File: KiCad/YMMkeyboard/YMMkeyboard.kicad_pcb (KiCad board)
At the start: 2 copper layers, 100 x 100 mm, 65 parts, among them J2 Conn_01x09, J3 Conn_01x09, SW10 SW_Push, SW11 SW_Push, SW12 SW_Push, SW13 SW_Push, SW14 SW_Push, SW15 SW_Push, SW16 SW_Push, SW17 SW_Push, SW18 SW_Push, SW19 SW_Push, SW2 SW_Push, SW20 SW_Push, SW21 SW_Push, SW22 SW_Push, SW23 SW_Push, SW24 SW_Push, SW25 SW_Push, SW26 SW_Push, SW27 SW_Push, SW28 SW_Push, SW29 SW_Push, SW3 SW_Push, SW30 SW_Push, SW31 SW_Push, SW32 RotaryEncoder_Switch, SW4 SW_Push, SW5 SW_Push, SW6 SW_Push, SW7 SW_Push, SW8 SW_Push, SW9 SW_Push

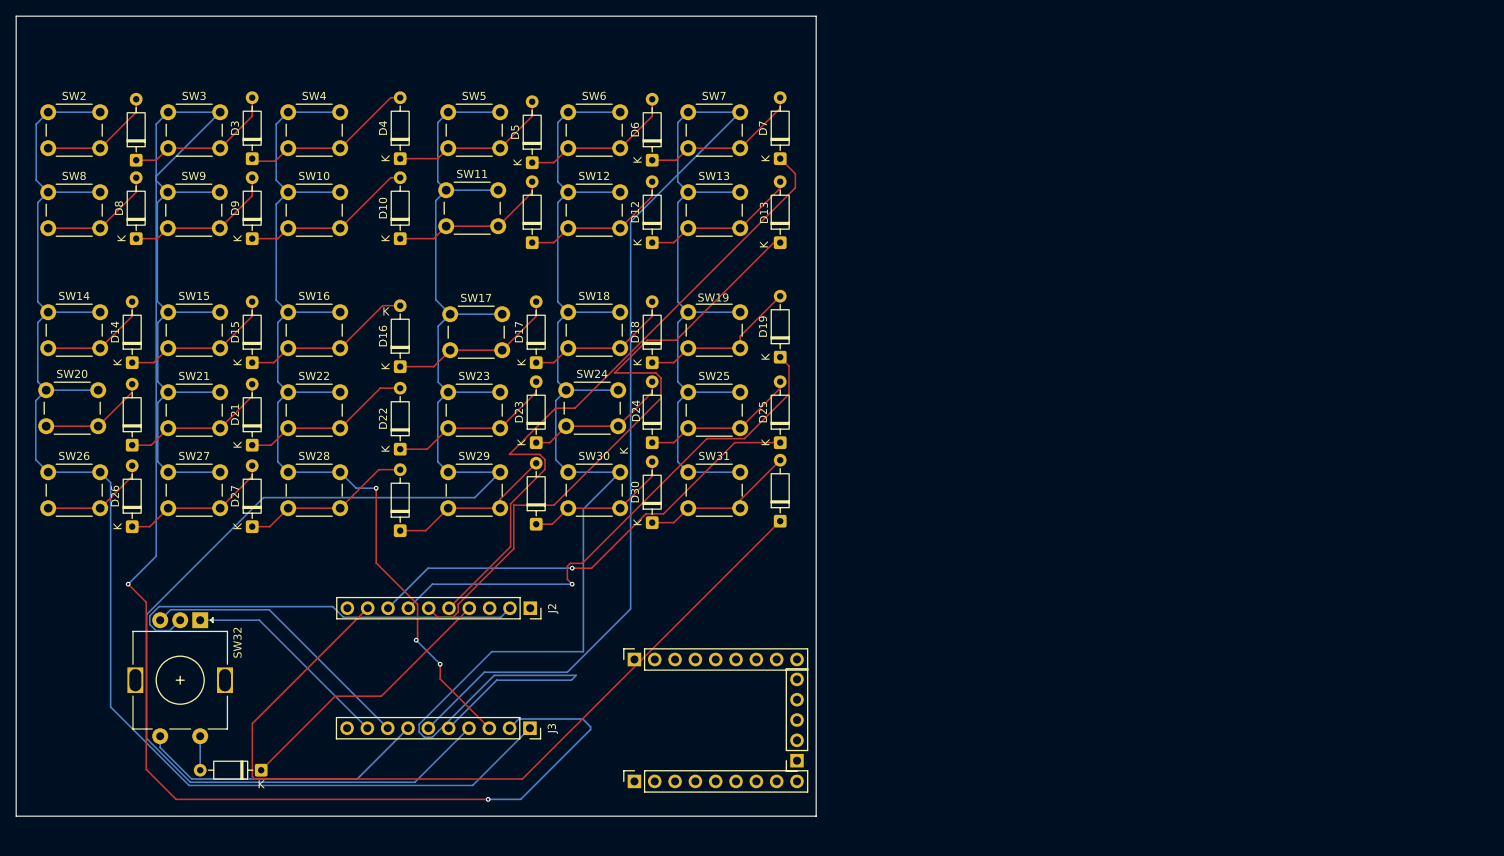
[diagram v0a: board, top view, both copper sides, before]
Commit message: キーボードの設計ミスを変更 原因:ダイオードを直列に配置した結果電圧降下した
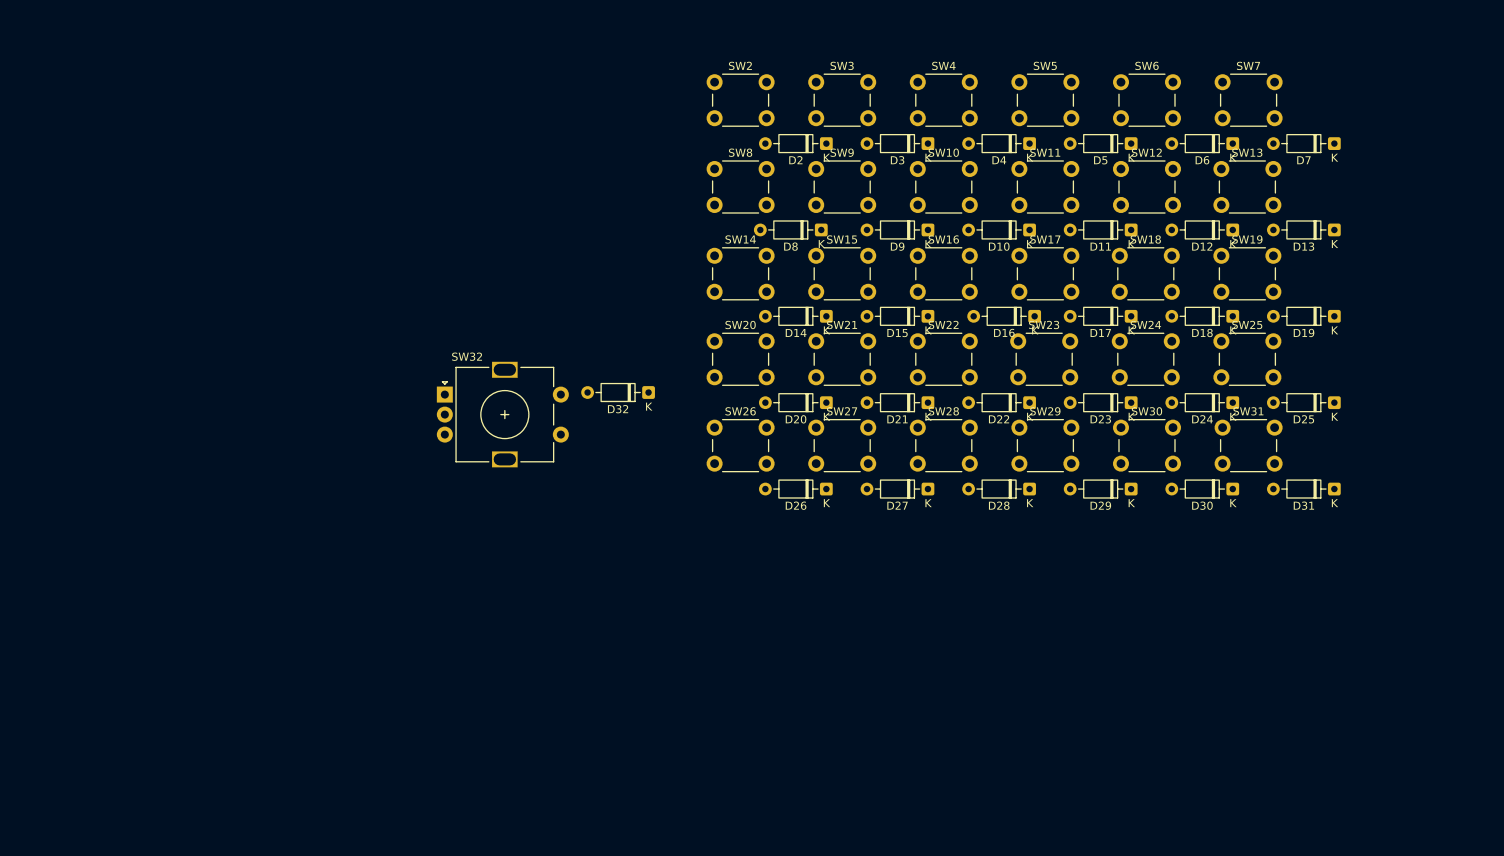
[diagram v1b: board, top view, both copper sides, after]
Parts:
- removed J2, J3: Conn_01x09, Connector_PinSocket_2.54mm:PinSocket_1x10_P2.54mm_Vertical
- removed REF**: RP2040-ZeroSocket, RP2040-ZeroSocket:RP2040-ZeroSocket
- moved D14 87.0 mm to (128.3, 56.5), turned to 180 degrees
- moved D20 86.9 mm to (128.3, 67.3), turned to 180 degrees
- moved D26 86.9 mm to (128.3, 78.1), turned to 180 degrees
- moved D2 86.3 mm to (128.3, 34.9), turned to 180 degrees
- moved D8 85.6 mm to (127.6, 45.7), turned to 180 degrees
- moved D15 84.7 mm to (141.0, 56.5), turned to 180 degrees
- moved D21 84.6 mm to (141.0, 67.3), turned to 180 degrees
- moved D27 84.6 mm to (141.0, 78.1), turned to 180 degrees
- moved D3 84.5 mm to (141.0, 34.9), turned to 180 degrees
- moved D9 84.5 mm to (141.0, 45.7), turned to 180 degrees
- moved SW20 83.8 mm to (114.3, 59.6)
- moved SW14 83.6 mm to (114.3, 49.0)
- moved SW26 83.5 mm to (114.3, 70.4)
- moved SW2 83.4 mm to (114.3, 27.2)
- moved SW8 83.4 mm to (114.3, 38.1)
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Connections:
- SW32 pad C: Net-(J2-Pin_2) -> GND
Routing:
- net Net-(SW15-Pad1): track 241.9 -> 0.00 mm, vias 2 -> 0
- net Net-(SW11-Pad1): track 194.4 -> 0.00 mm
- net Net-(SW13-Pad1): track 181.0 -> 0.00 mm
- net Net-(SW12-Pad1): track 173.2 -> 0.00 mm
- net Net-(SW14-Pad1): track 171.3 -> 0.00 mm
- net Net-(SW10-Pad1): track 123.5 -> 0.00 mm, vias 3 -> 0
- net Net-(D31-K): track 106.5 -> 0.00 mm
- net Net-(D7-K): track 82.3 -> 0.00 mm
- net Net-(D13-K): track 80.6 -> 0.00 mm
- net Net-(D19-K): track 65.9 -> 0.00 mm, vias 1 -> 0
- net Net-(D25-K): track 57.6 -> 0.00 mm, vias 1 -> 0
- net Net-(J2-Pin_2): track 52.3 -> 0.00 mm
- net Net-(SW32-PadS1): track 36.7 -> 0.00 mm
- net Net-(SW32-PadB): track 35.1 -> 0.00 mm
- net Net-(D32-K): track 34.4 -> 0.00 mm
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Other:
- board outline removed

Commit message: 2号機発注データ
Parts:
- removed the D29 at (166.4, 78.1)
- added D29: 1N4148, Diode_THT:D_DO-35_SOD27_P7.62mm_Horizontal, F.Cu at (175.2, 92.0)
- added D29: 1N4148, Diode_THT:D_DO-35_SOD27_P7.62mm_Horizontal, F.Cu at (174.3, 65.1)
- added J1: OLED, Connector_PinSocket_2.54mm:PinSocket_1x05_P2.54mm_Vertical, F.Cu at (167.0, 81.9)
- added J3: RGB, Connector_PinSocket_2.54mm:PinSocket_1x03_P2.54mm_Vertical, F.Cu at (204.0, 83.5)
- added REF**: KEY_SWITCH, isw-kbd:CherryMX_Hotswap_1u, F.Cu at (181.0, 87.0)
- added U1: RP2040-Zero, RP2040-ZeroSocket:RP2040-ZeroSocket, F.Cu at (125.7, 108.3)
- moved SW32 113.8 mm to (186.5, 108.0)
- moved D32 113.5 mm to (208.0, 116.0), turned to 90 degrees
- moved D31 17.4 mm to (203.3, 65.1), turned to -90 degrees
- moved D25 16.8 mm to (203.3, 55.1), turned to -90 degrees
- moved D30 16.6 mm to (189.3, 65.1), turned to -90 degrees
- moved D19 16.2 mm to (203.3, 45.1), turned to -90 degrees
- moved SW25 16.0 mm to (193.5, 57.2)
- moved SW31 16.0 mm to (193.5, 67.3)
- moved D24 15.9 mm to (189.3, 55.1), turned to -90 degrees
- moved SW19 15.9 mm to (193.5, 47.0)
- moved SW13 15.9 mm to (193.5, 36.8)
- moved SW7 15.7 mm to (193.5, 26.7)
- moved D13 15.5 mm to (203.0, 35.0), turned to -90 degrees
- moved D18 15.3 mm to (189.3, 45.1), turned to -90 degrees
- moved D7 15.2 mm to (203.3, 25.1), turned to -90 degrees
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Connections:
- D11 pad 1: Net-(D11-K) -> Net-(D10-K)
- D11 pad 2: Net-(D10-K) -> Net-(D11-A)
- D12 pad 1: Net-(D12-K) -> Net-(D10-K)
- D12 pad 2: Net-(D11-K) -> Net-(D12-A)
- D13 pad 1: Net-(D13-K) -> Net-(D10-K)
- D13 pad 2: Net-(D12-K) -> Net-(D13-A)
- D15 pad 1: Net-(D15-K) -> Net-(D14-K)
- D15 pad 2: Net-(D14-K) -> Net-(D15-A)
- D16 pad 1: Net-(D16-K) -> Net-(D14-K)
- D16 pad 2: Net-(D15-K) -> Net-(D16-A)
- D17 pad 1: Net-(D17-K) -> Net-(D14-K)
- D17 pad 2: Net-(D16-K) -> Net-(D17-A)
- D18 pad 1: Net-(D18-K) -> Net-(D14-K)
- D18 pad 2: Net-(D17-K) -> Net-(D18-A)
- D19 pad 1: Net-(D19-K) -> Net-(D14-K)
- D19 pad 2: Net-(D18-K) -> Net-(D19-A)
- D21 pad 1: Net-(D21-K) -> Net-(D20-K)
- D21 pad 2: Net-(D20-K) -> Net-(D21-A)
- D22 pad 1: Net-(D22-K) -> Net-(D20-K)
- D22 pad 2: Net-(D21-K) -> Net-(D22-A)
- D23 pad 1: Net-(D23-K) -> Net-(D20-K)
- D23 pad 2: Net-(D22-K) -> Net-(D23-A)
- D24 pad 1: Net-(D24-K) -> Net-(D20-K)
- D24 pad 2: Net-(D23-K) -> Net-(D24-A)
- D25 pad 1: Net-(D25-K) -> Net-(D20-K)
- D25 pad 2: Net-(D24-K) -> Net-(D25-A)
- D27 pad 1: Net-(D27-K) -> Net-(D26-K)
- D27 pad 2: Net-(D26-K) -> Net-(D27-A)
- D28 pad 1: Net-(D28-K) -> Net-(D26-K)
- D28 pad 2: Net-(D27-K) -> Net-(D28-A)
- D3 pad 1: Net-(D3-K) -> Net-(D2-K)
- D3 pad 2: Net-(D2-K) -> Net-(D3-A)
- D30 pad 1: Net-(D30-K) -> Net-(D26-K)
- D31 pad 1: Net-(D31-K) -> Net-(D26-K)
- D31 pad 2: Net-(D30-K) -> Net-(D31-A)
- D4 pad 1: Net-(D4-K) -> Net-(D2-K)
- D4 pad 2: Net-(D3-K) -> Net-(D4-A)
- D5 pad 1: Net-(D5-K) -> Net-(D2-K)
- D5 pad 2: Net-(D4-K) -> Net-(D5-A)
- D6 pad 1: Net-(D6-K) -> Net-(D2-K)
- D6 pad 2: Net-(D5-K) -> Net-(D6-A)
- D7 pad 1: Net-(D7-K) -> Net-(D2-K)
- D7 pad 2: Net-(D6-K) -> Net-(D7-A)
- D8 pad 1: Net-(D8-K) -> Net-(D10-K)
- D9 pad 1: Net-(D10-A) -> Net-(D10-K)
- D9 pad 2: Net-(D8-K) -> Net-(D9-A)
- SW11 pad 2: Net-(D10-K) -> Net-(D11-A)
- SW12 pad 2: Net-(D11-K) -> Net-(D12-A)
- SW13 pad 2: Net-(D12-K) -> Net-(D13-A)
- SW15 pad 2: Net-(D14-K) -> Net-(D15-A)
- SW16 pad 2: Net-(D15-K) -> Net-(D16-A)
- SW17 pad 2: Net-(D16-K) -> Net-(D17-A)
- SW18 pad 2: Net-(D17-K) -> Net-(D18-A)
- SW19 pad 2: Net-(D18-K) -> Net-(D19-A)
- SW21 pad 2: Net-(D20-K) -> Net-(D21-A)
- SW22 pad 2: Net-(D21-K) -> Net-(D22-A)
- SW23 pad 2: Net-(D22-K) -> Net-(D23-A)
- SW24 pad 2: Net-(D23-K) -> Net-(D24-A)
- SW25 pad 2: Net-(D24-K) -> Net-(D25-A)
- SW27 pad 2: Net-(D26-K) -> Net-(D27-A)
- SW28 pad 2: Net-(D27-K) -> Net-(D28-A)
- SW29 pad 2: Net-(D28-K) -> Net-(D29-A)
- SW3 pad 2: Net-(D2-K) -> Net-(D3-A)
- SW31 pad 2: Net-(D30-K) -> Net-(D31-A)
- SW4 pad 2: Net-(D3-K) -> Net-(D4-A)
- SW5 pad 2: Net-(D4-K) -> Net-(D5-A)
- SW6 pad 2: Net-(D5-K) -> Net-(D6-A)
- SW7 pad 2: Net-(D6-K) -> Net-(D7-A)
- SW9 pad 2: Net-(D8-K) -> Net-(D9-A)
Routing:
- net Net-(D2-K): track 0.00 -> 211.4 mm
- net Net-(D10-K): track 0.00 -> 199.7 mm
- net Net-(J1-Pin_2): track 0.00 -> 190.7 mm
- net Net-(D14-K): track 0.00 -> 188.0 mm
- net Net-(D20-K): track 0.00 -> 176.3 mm
- net Net-(SW13-Pad1): track 0.00 -> 175.6 mm
- net Net-(D26-K): track 0.00 -> 164.6 mm
- net Net-(SW12-Pad1): track 0.00 -> 158.3 mm
- net Net-(SW11-Pad1): track 0.00 -> 141.0 mm
- net Net-(SW10-Pad1): track 0.00 -> 126.6 mm
- net GND: track 0.00 -> 126.2 mm, vias 0 -> 3
- net Net-(SW15-Pad1): track 0.00 -> 116.6 mm
- net Net-(SW14-Pad1): track 0.00 -> 109.7 mm
- net Net-(J3-Pin_3): track 0.00 -> 96.4 mm
- net Net-(SW32-PadS1): track 0.00 -> 89.4 mm
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- added copper zone on F.Cu, net (none)
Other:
- board outline added: 100 x 100 mm
- board text added: "USB"
